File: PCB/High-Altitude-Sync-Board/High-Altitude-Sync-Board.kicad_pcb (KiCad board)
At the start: 4 copper layers, 48 x 58 mm, 51 parts, among them J1 USB_C_Receptacle_USB2.0_14P, J17 VN100T-UPDATE, J18 Conn_01x02, J19 Conn_01x02, J2 UBLOX_TRIGGER, J20 EXT_SYNC, J23 Conn_01x04, J24 SWD, J25 Conn_01x04, J26 UART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

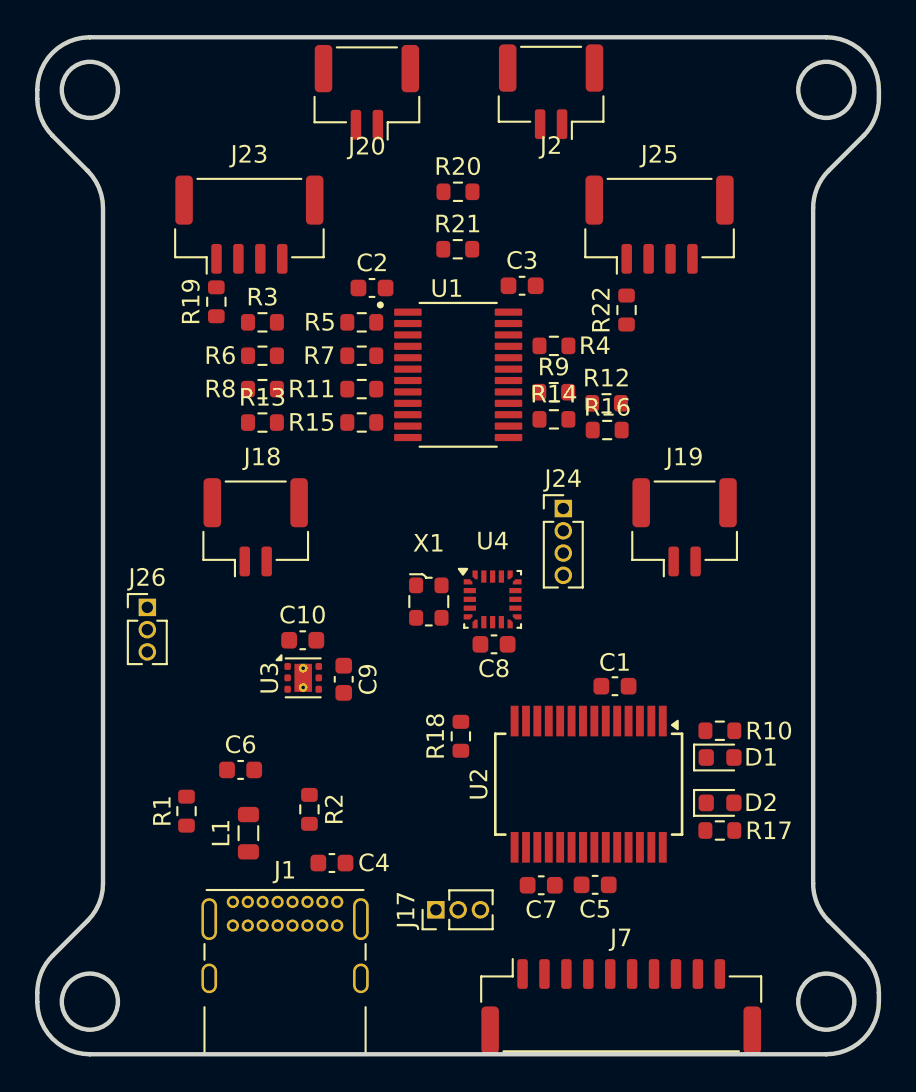
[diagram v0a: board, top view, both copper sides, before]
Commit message: Routed RS232
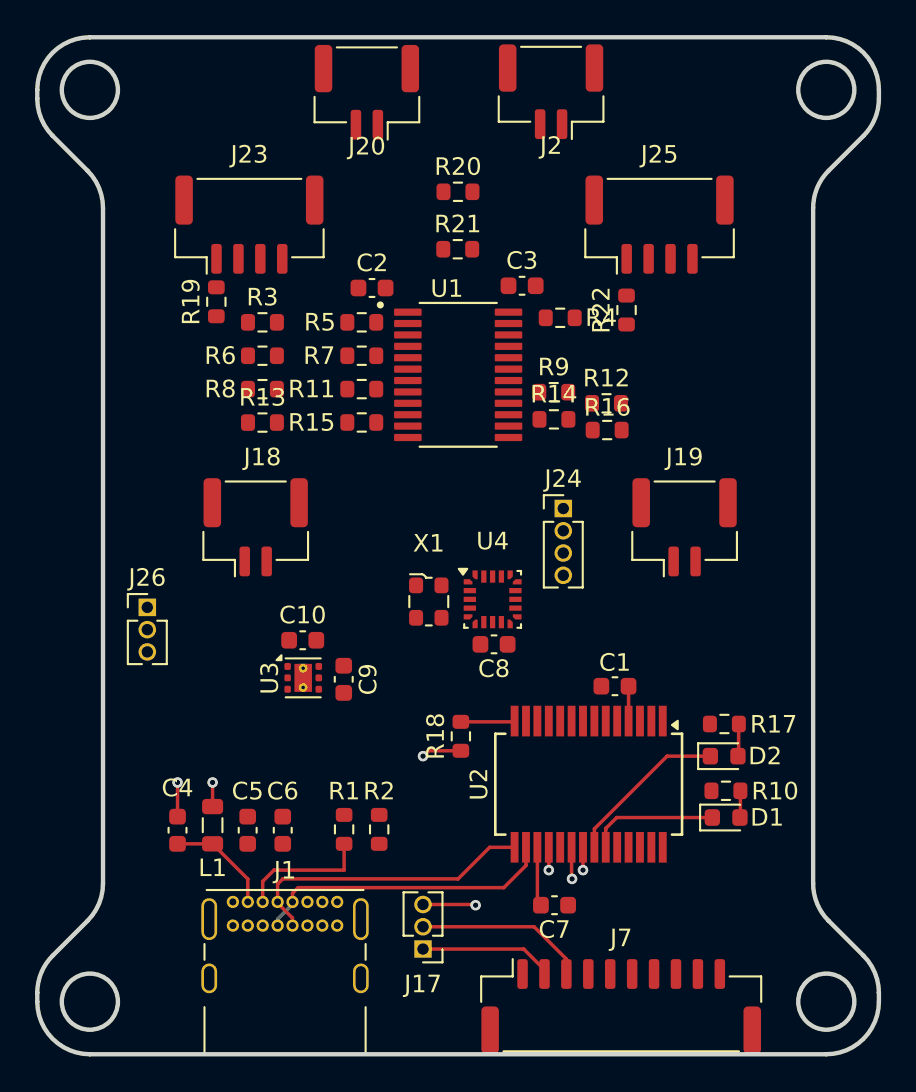
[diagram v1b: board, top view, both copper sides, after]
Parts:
- moved C5 20.1 mm to (103.0, 106.7), turned to 90 degrees
- moved R1 9.05 mm to (108.5, 106.7)
- moved C4 9.00 mm to (99.0, 106.7), turned to 90 degrees
- moved R17 6.08 mm to (130.2, 100.7)
- moved C6 4.20 mm to (105.0, 106.7), turned to 90 degrees
- moved R2 4.14 mm to (110.5, 106.7)
- moved R10 3.44 mm to (130.3, 104.5)
- moved D1 3.44 mm to (130.3, 106.0)
- moved D2 2.68 mm to (130.2, 102.5)
- moved J17 2.36 mm to (113.0, 113.5), turned to 180 degrees
- moved L1 2.09 mm to (101.0, 106.4), turned to -90 degrees
- moved R4 1.64 mm to (120.8, 77.5)
- moved C7 1.37 mm to (120.5, 111.0)
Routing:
- net Net-(U2-USBD-): track 0.00 -> 17.2 mm
- net Net-(U2-USBD+): track 0.00 -> 17.1 mm
- net /VN-100T-RX1: track 0.00 -> 9.79 mm
- net Net-(D2-K): track 0.00 -> 9.38 mm
- net /VN-100T-TX1: track 0.00 -> 7.66 mm
- net Net-(J1-CC1): track 0.00 -> 7.58 mm
- net GND: track 0.00 -> 7.57 mm, vias 0 -> 4
- net Net-(D1-K): track 0.00 -> 7.41 mm
- net Net-(C4-Pad1): track 0.00 -> 6.14 mm
- net +3V3: track 0.00 -> 4.27 mm, vias 0 -> 1
- net Net-(U2-3V3OUT): track 0.00 -> 3.47 mm
- net +5V: track 0.00 -> 3.19 mm, vias 0 -> 2
- net Net-(U2-CBUS3): track 0.00 -> 3.08 mm
- net Net-(D2-A): track 0.00 -> 1.84 mm
- net Net-(D1-A): track 0.00 -> 1.54 mm

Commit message: Routed top part of the sync board
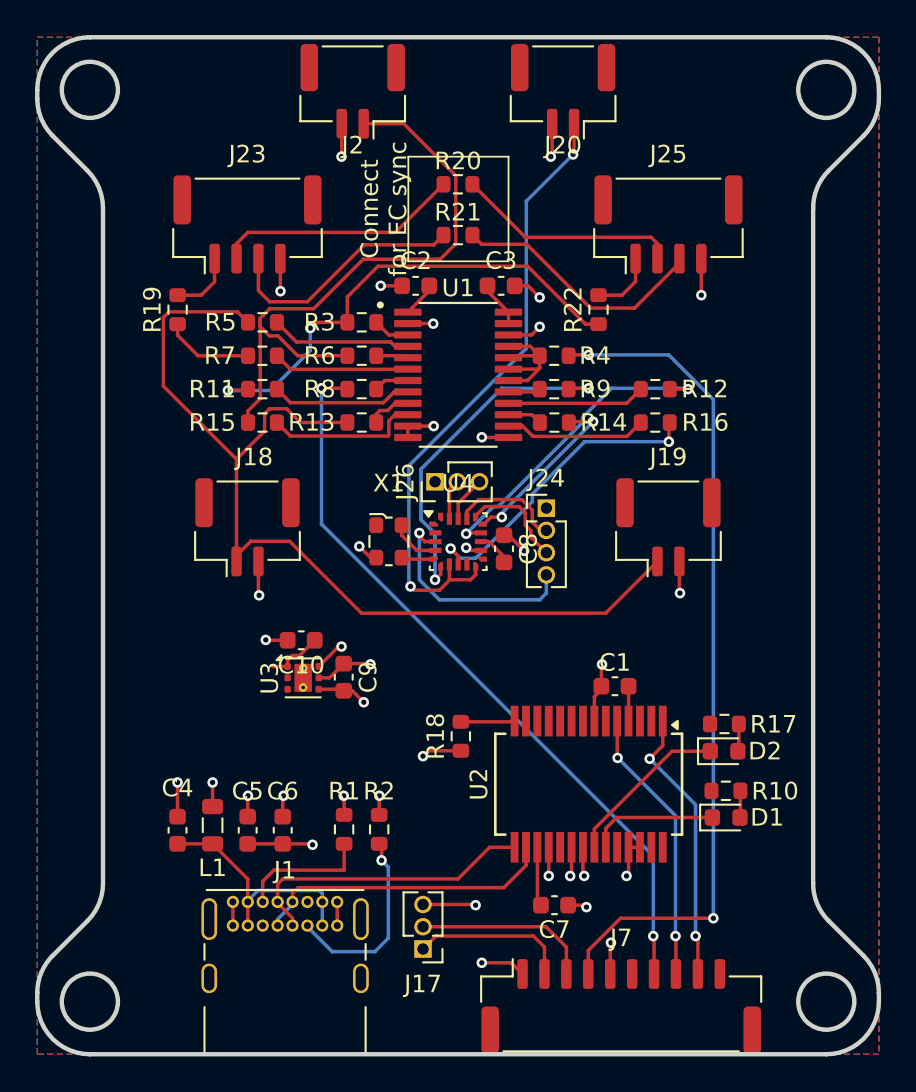
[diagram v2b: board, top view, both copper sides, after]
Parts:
- moved J26 17.9 mm to (113.7, 86.9), turned to 90 degrees
- moved J2 11.3 mm to (109.0, 64.6)
- moved J20 11.2 mm to (121.0, 64.6)
- moved R13 5.66 mm to (109.5, 83.5)
- moved R15 5.66 mm to (103.8, 83.5)
- moved R11 5.66 mm to (103.8, 81.6)
- moved R8 5.66 mm to (109.5, 81.6)
- moved R6 5.66 mm to (109.5, 79.7)
- moved R7 5.66 mm to (103.8, 79.7)
- moved R3 5.66 mm to (109.5, 77.8)
- moved R5 5.66 mm to (103.8, 77.8)
- moved C8 5.48 mm to (117.6, 90.7), turned to 90 degrees
- moved X1 4.12 mm to (111.1, 90.3)
- moved U4 3.83 mm to (115.0, 90.3)
- moved R12 2.90 mm to (126.2, 81.6)
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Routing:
- net /FLIR_TRIGGER_IN: track 0.00 -> 56.9 mm
- net /VN-100T-SYNC-OUT: track 0.00 -> 48.1 mm, vias 0 -> 2
- net GND: track 7.57 -> 54.1 mm, vias 4 -> 29
- net /VN-100T-SYNC-IN: track 0.00 -> 42.8 mm, vias 0 -> 2
- net /EXT_SYNC: track 0.00 -> 35.8 mm, vias 0 -> 2
- net /UBLOX_TRIGGER_IN: track 0.00 -> 35.6 mm
- net /EC_1_TRIGGER_IN: track 0.00 -> 28.2 mm, vias 0 -> 2
- net /TIM2_CH2: track 0.00 -> 20.1 mm, vias 0 -> 2
- net /TIM21_CH2: track 0.00 -> 18.3 mm, vias 0 -> 2
- net /TIM2_CH1: track 0.00 -> 17.9 mm, vias 0 -> 2
- net /VN-100T-RX2_TTL: track 0.00 -> 15.9 mm, vias 0 -> 2
- net /VN-100T-TX2_TTL: track 0.00 -> 15.8 mm, vias 0 -> 2
- net /SYNC_OUT_N2: track 0.00 -> 14.9 mm
- net /SYNC_IN_N4: track 0.00 -> 14.2 mm
- net /SYNC_IN_P3: track 0.00 -> 14.1 mm
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- added copper zone on B.Cu, net +3V3
- added copper zone on F.Cu, net +3V3
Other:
- board text added: "Connect for EC sync"

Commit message: Almost final routing of High Altitude Sync Board
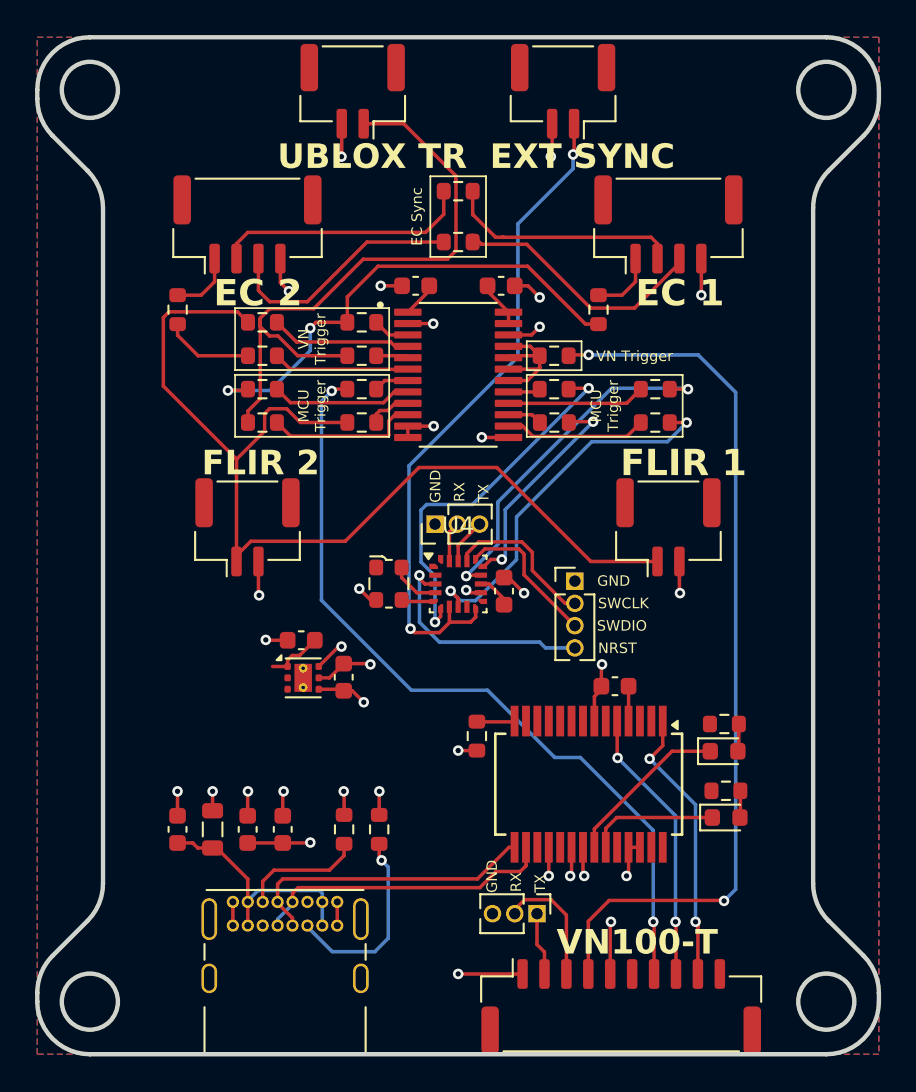
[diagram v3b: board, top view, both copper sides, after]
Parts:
- removed C7: 100nF, Capacitor_SMD:C_0603_1608Metric
- moved J17 6.81 mm to (119.5, 111.5), turned to -90 degrees
- moved J24 4.47 mm to (121.7, 92.5)
- moved C8 2.41 mm to (117.6, 93.1)
- moved J26 2.41 mm to (113.7, 89.3)
- moved U4 2.41 mm to (115.0, 92.7)
- moved X1 2.41 mm to (111.1, 92.7)
- moved R18 0.91 mm to (116.1, 101.4)
- moved R21 0.39 mm to (115.0, 73.2)
- moved R20 0.39 mm to (115.0, 70.3)
- moved L1 0.24 mm to (101.0, 106.7)
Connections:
- U2 pad 17: Net-(U2-3V3OUT) -> unconnected-(U2-3V3OUT-Pad17)
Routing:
- net /VN-100T-TX1: track 9.03 -> 3.64 mm
- net /TIM2_CH1: track 17.9 -> 21.4 mm
- net Net-(U2-3V3OUT): track 3.47 -> 0.00 mm
- net /VN-100T-SYNC-IN: track 42.8 -> 45.8 mm
- net /VN-100T-SYNC-OUT: track 48.1 -> 51.0 mm
- net /SWCLK: track 6.37 -> 8.93 mm
- net /SWDIO: track 5.96 -> 8.38 mm
- net /EXT_SYNC: track 35.8 -> 38.2 mm
- net /TIM21_CH1: track 10.2 -> 12.6 mm
- net /VN-100T-RX1: track 10.2 -> 7.80 mm
- net GND: track 54.1 -> 51.8 mm, vias 29 -> 27
- net /TIM21_CH2: track 18.3 -> 20.5 mm
- net +3V3: track 17.0 -> 15.8 mm
- net /TIM2_CH2: track 20.1 -> 21.2 mm
- net /FLIR_TRIGGER_IN: track 56.9 -> 57.9 mm
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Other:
- board text added: "EC 1"
- board text added: "EC 2"
- board text added: "EC Sync"
- board text added: "EXT SYNC"
- board text added: "FLIR 1"
- board text added: "FLIR 2"
- board text added: "GND"
- board text added: "IMPORTANT: This board has TWO operating modes. Pick ONLY one of them. # Using the VNAV as clock source -> Short {dblquote}VN Trigger{dblquote} The SYNC_OUT pin of the VNAV generates a trigger. **All the cameras are connected together** and thus all the trigger signals are the same. No GPS sync. # Using an external or MCU clock source -> Short {dblquote}MCU Trigger{dblquote} We generate a clock so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"
- board text added: "Kumar Robotics - EC Synchronization Board fclad@seas.upenn.edu"
- board text added: "MCU Trigger"
- board text added: "NRST"
- board text added: "RX"
- board text added: "SWCLK"
- board text added: "SWDIO"
- board text added: "TX"
- board text added: "UBLOX TR"
- board text added: "VN Trigger"
- board text added: "VN100-T"
- board text removed: "Connect for EC sync"

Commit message: High Altitude Sync Board - V1
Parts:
- removed C8: 100nF, Capacitor_SMD:C_0603_1608Metric
- added C7: 100nF, Capacitor_SMD:C_0603_1608Metric, F.Cu at (118.0, 92.9)
- added TP1: 5V TP, TestPoint:TestPoint_THTPad_1.0x1.0mm_Drill0.5mm, F.Cu at (107.4, 102.4)
- added TP2: GND TP, TestPoint:TestPoint_THTPad_1.0x1.0mm_Drill0.5mm, F.Cu at (102.8, 102.4)
- added TP3: 3V3 TP, TestPoint:TestPoint_THTPad_1.0x1.0mm_Drill0.5mm, F.Cu at (105.1, 102.4)
- J18, J19: value Conn_01x02 -> BM02B-GHS-TBT
- J2: value UBLOX_TRIGGER -> SM02B-GHS-TB
- J20: value EXT_SYNC -> SM02B-GHS-TB
- J23, J25: value Conn_01x04 -> BM04B-GHS-TBT
- R11, R12, R13, R14, R15, R16, R20, R21, R8, R9: value DNP -> 0R
- moved J24 6.51 mm to (116.8, 96.9), turned to -90 degrees
- moved R18 5.03 mm to (120.2, 98.5), turned to 180 degrees
- moved J1 0.51 mm to (102.2, 110.3)
- moved J7 0.39 mm to (124.3, 116.4)
- moved C4 0.34 mm to (99.3, 106.7)
- moved C5 0.34 mm to (103.3, 106.7)
- moved C6 0.34 mm to (105.3, 106.7)
- moved L1 0.34 mm to (101.3, 106.7)
- moved R1 0.34 mm to (108.8, 106.7)
- moved R2 0.34 mm to (110.8, 106.7)
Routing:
- net /NRST: track 13.4 -> 6.01 mm
- net /SWCLK: track 8.93 -> 14.4 mm, vias 0 -> 1
- net /SWDIO: track 8.38 -> 12.9 mm, vias 0 -> 1
- net +3V3: track 15.8 -> 14.8 mm, vias 1 -> 0
- net Net-(C4-Pad1): track 14.4 -> 13.6 mm
- net /TIM21_CH2: track 20.5 -> 21.3 mm
- net GND: track 51.8 -> 52.5 mm
- net Net-(U2-CBUS3): track 2.17 -> 2.77 mm
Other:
- board text added: "3V3"
- board text added: "5V"
- board text added: "V1 2924"
